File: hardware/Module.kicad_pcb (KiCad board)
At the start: 2 copper layers, 99.1 x 109.2 mm, 71 parts, among them J1 In, J13 Power, J2 Impulse, J3 Left, J4 Right, J5 Ctrl1, J6 Ctrl2, J7 Ctrl3, J8 Ctrl4, J9 I2C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

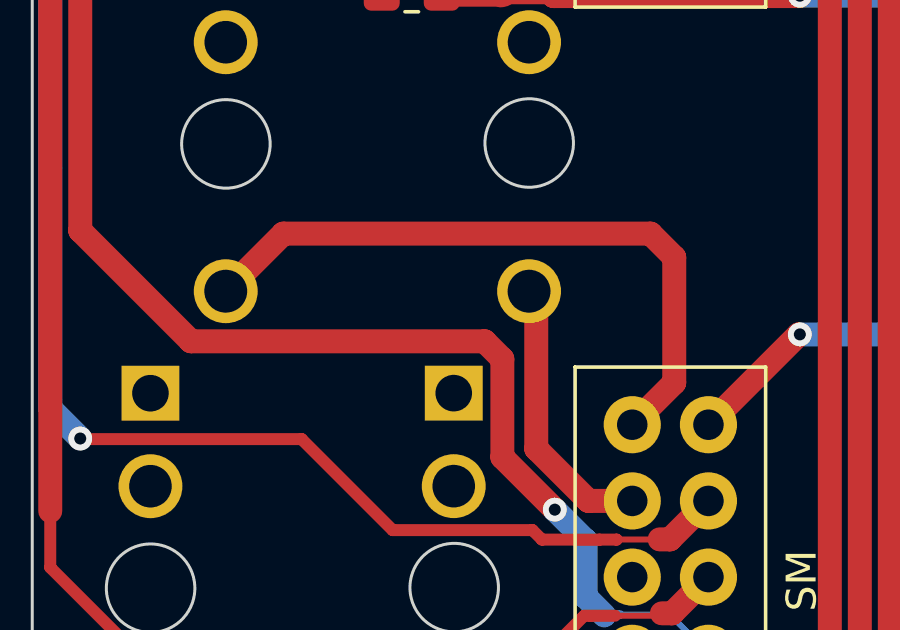
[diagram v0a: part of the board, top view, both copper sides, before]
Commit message: Move impulse farther from input
Signed-off-by: Petr Horacek <petr@zlosynth.com>
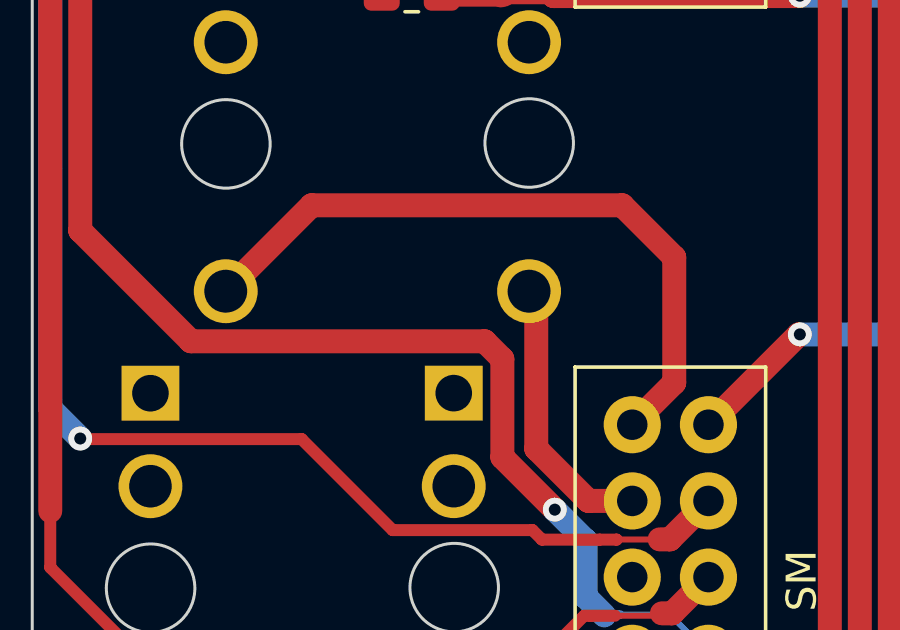
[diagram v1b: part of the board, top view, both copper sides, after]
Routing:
- net IMPULSE: track 22.2 -> 23.0 mm
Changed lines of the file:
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@@
 	)
 	(segment
-		(start 55.44 122.79)
-		(end 53.52 124.71)
+		(start 56.383873 121.846127)
+		(end 66.736127 121.846127)
 		(width 0.8)
 		(layer "F.Cu")
@@
 	)
 	(segment
-		(start 67.07 129.16)
+		(start 68.47 127.76)
+		(end 67.07 129.16)
+		(width 0.8)
+		(layer "F.Cu")
+		(net 42)
+	)
+	(segment
+		(start 68.47 123.58)
 		(end 68.47 127.76)
 		(width 0.8)
@@
 	)
 	(segment
-		(start 68.47 127.76)
-		(end 68.47 123.58)
+		(start 53.52 124.71)
+		(end 56.383873 121.846127)
 		(width 0.8)
 		(layer "F.Cu")
@@
 	)
 	(segment
-		(start 68.47 123.58)
-		(end 67.68 122.79)
+		(start 66.736127 121.846127)
+		(end 68.47 123.58)
 		(width 0.8)
 		(layer "F.Cu")
-		(net 42)
-	)
-	(segment
-		(start 55.44 122.79)
-		(end 67.68 122.79)
-		(width 0.8)
-		(layer "F.Cu")
